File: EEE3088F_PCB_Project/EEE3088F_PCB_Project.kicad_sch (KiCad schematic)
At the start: 44 parts, among them IC1 DRV8833PWPR, IC2 DRV8833PWPR, IC3 TPS62067DSGR, IC4 TPS62067DSGR, IC5 INA219AIDCNR, J1 Conn_02x16_Odd_Even, Q3 MMBT2222A, Q4 MMBT2222A, Q5 AO3401A, Q6 AO3401A

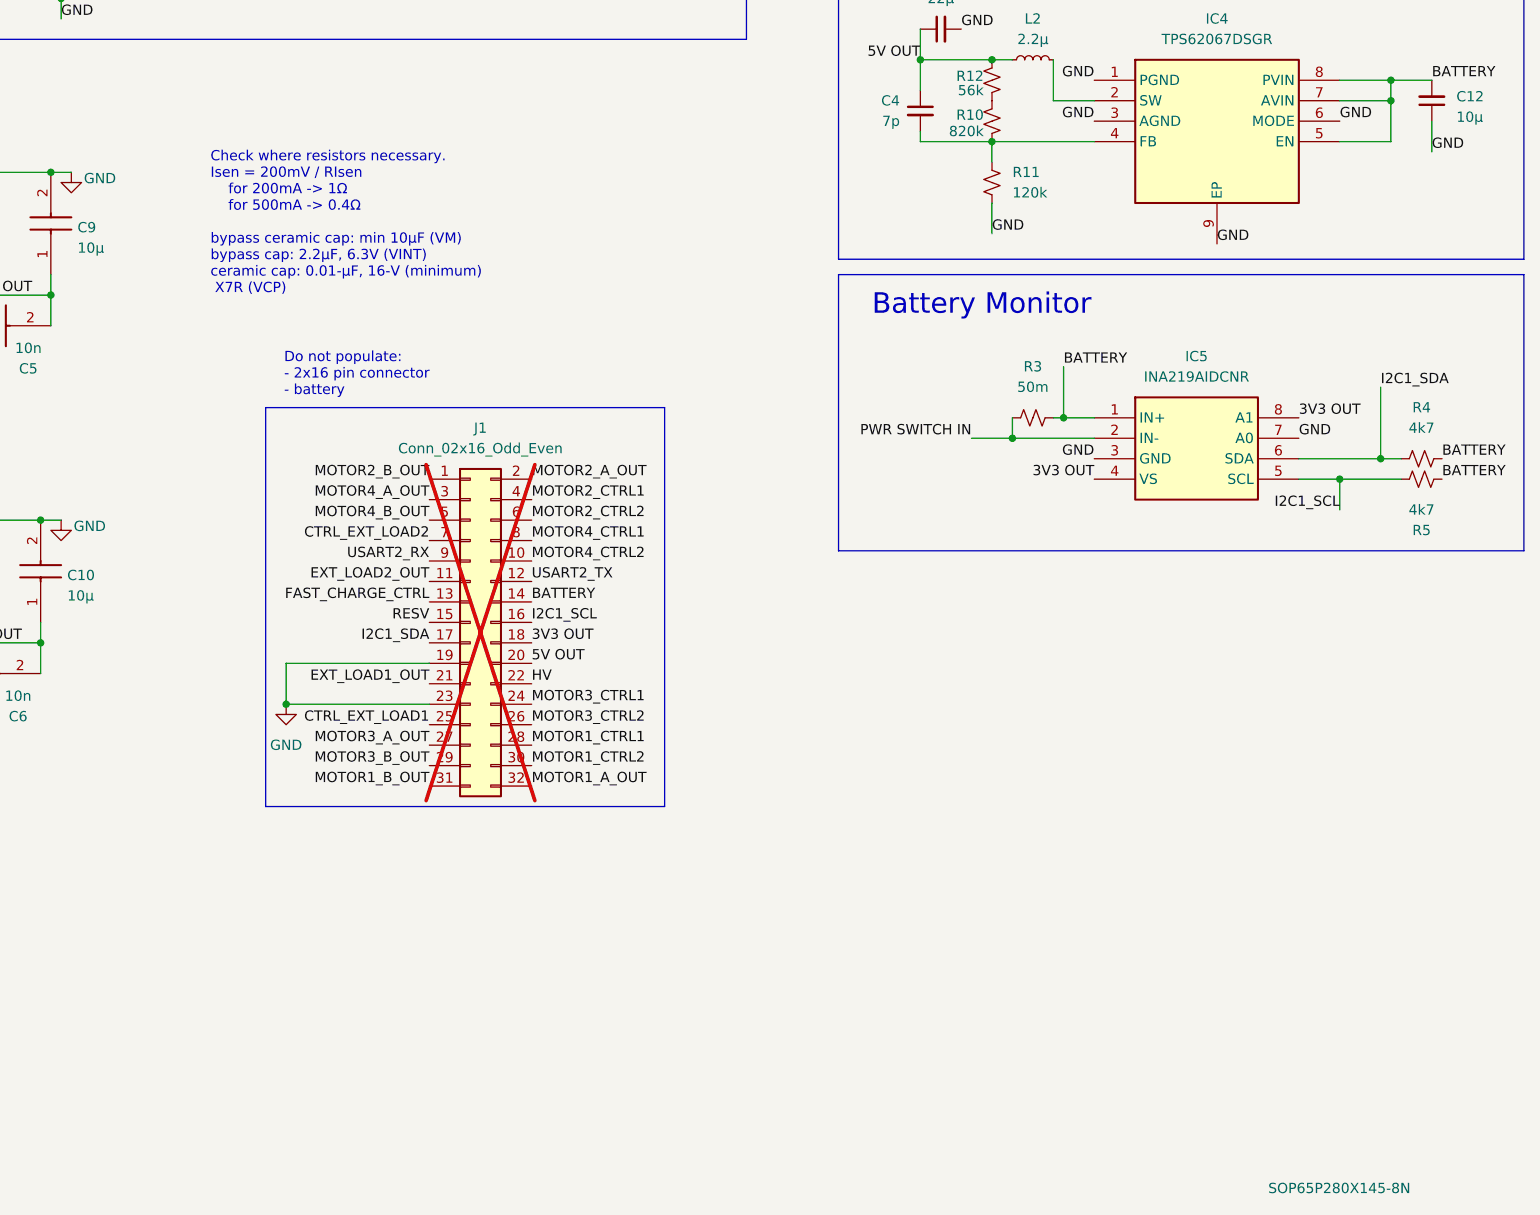
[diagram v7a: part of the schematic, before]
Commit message: v0.6.1
Lula: starting to update battery monitor circuit
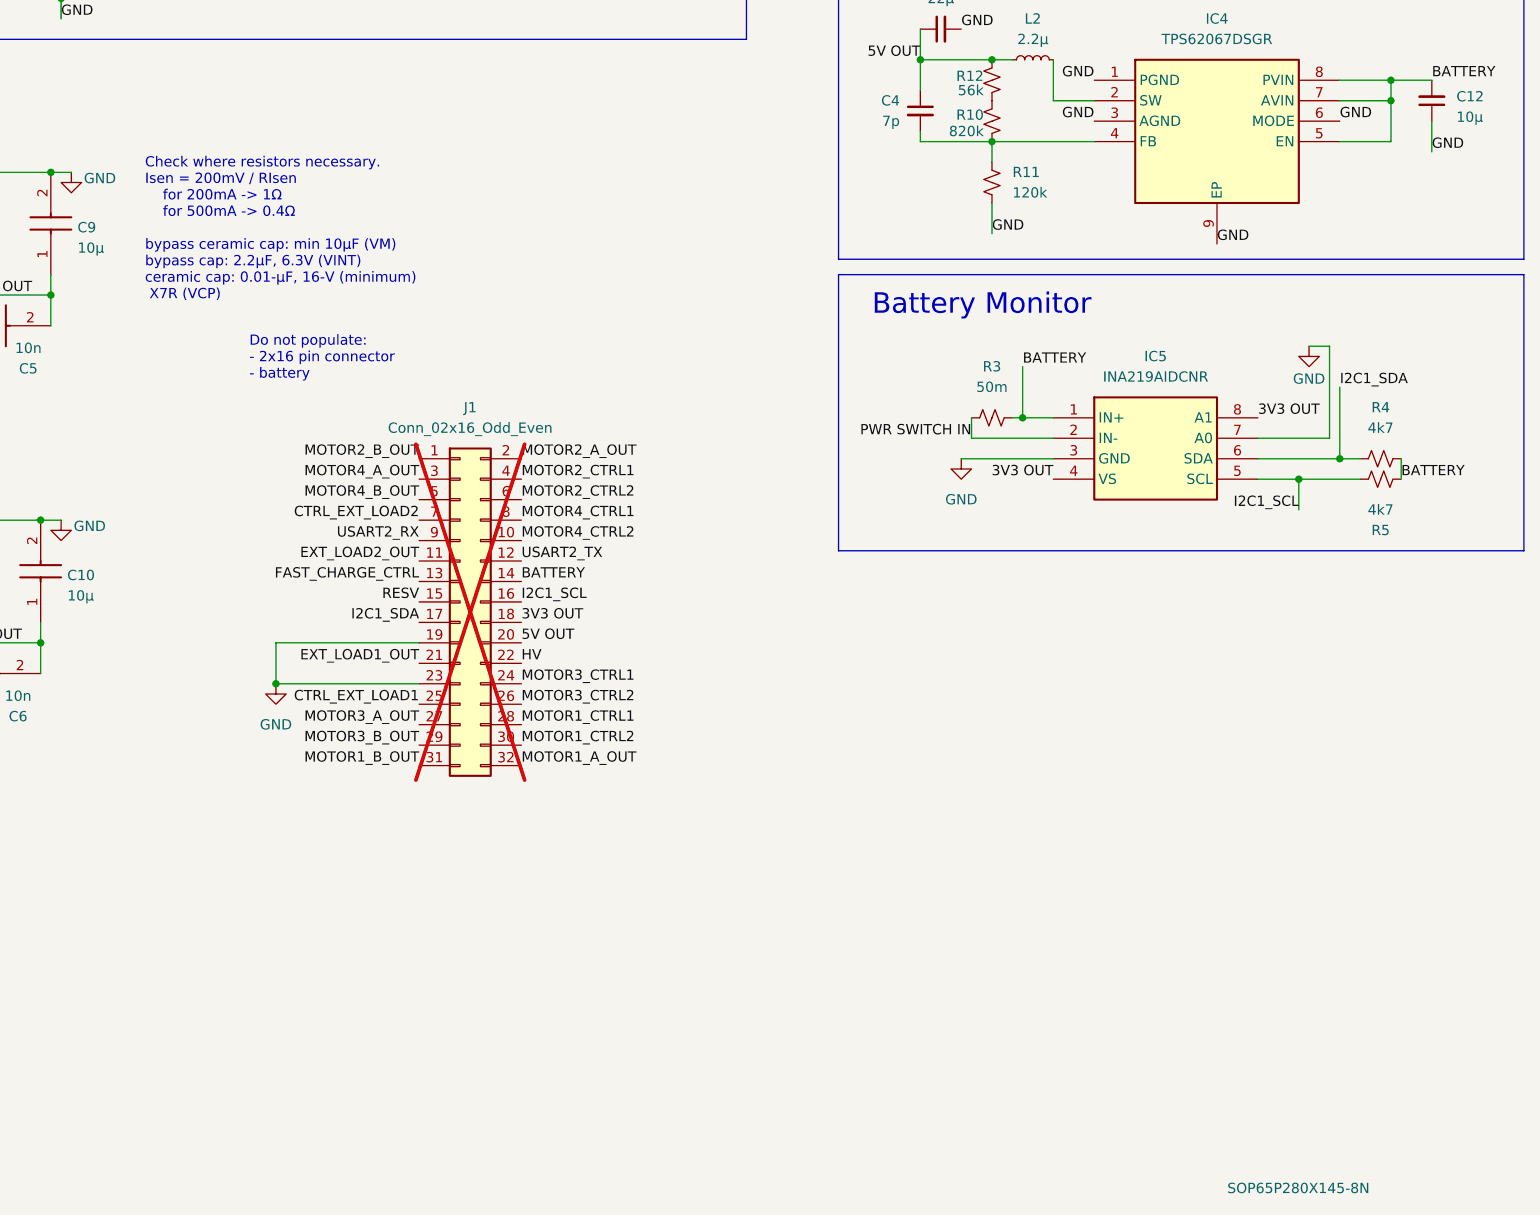
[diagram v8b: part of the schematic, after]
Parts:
- J1: footprint Connector_Samtec_HLE_THT:Samtec_HLE-116-02-xx-DV-TE_2x16_P2.54mm_Horizontal -> Connector_PinSocket_2.54mm:PinSocket_2x16_P2.54mm_Vertical
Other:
- moved on the sheet: IC5, J1, R3, R4, R5
